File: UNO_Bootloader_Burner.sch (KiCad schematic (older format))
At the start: 12 parts, among them J1 Conn_01x06_Female, J2 Conn_01x06_Female, U1 ATmega328-AU-MCU_Microchip_AT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, Y1 Crystal_GND24

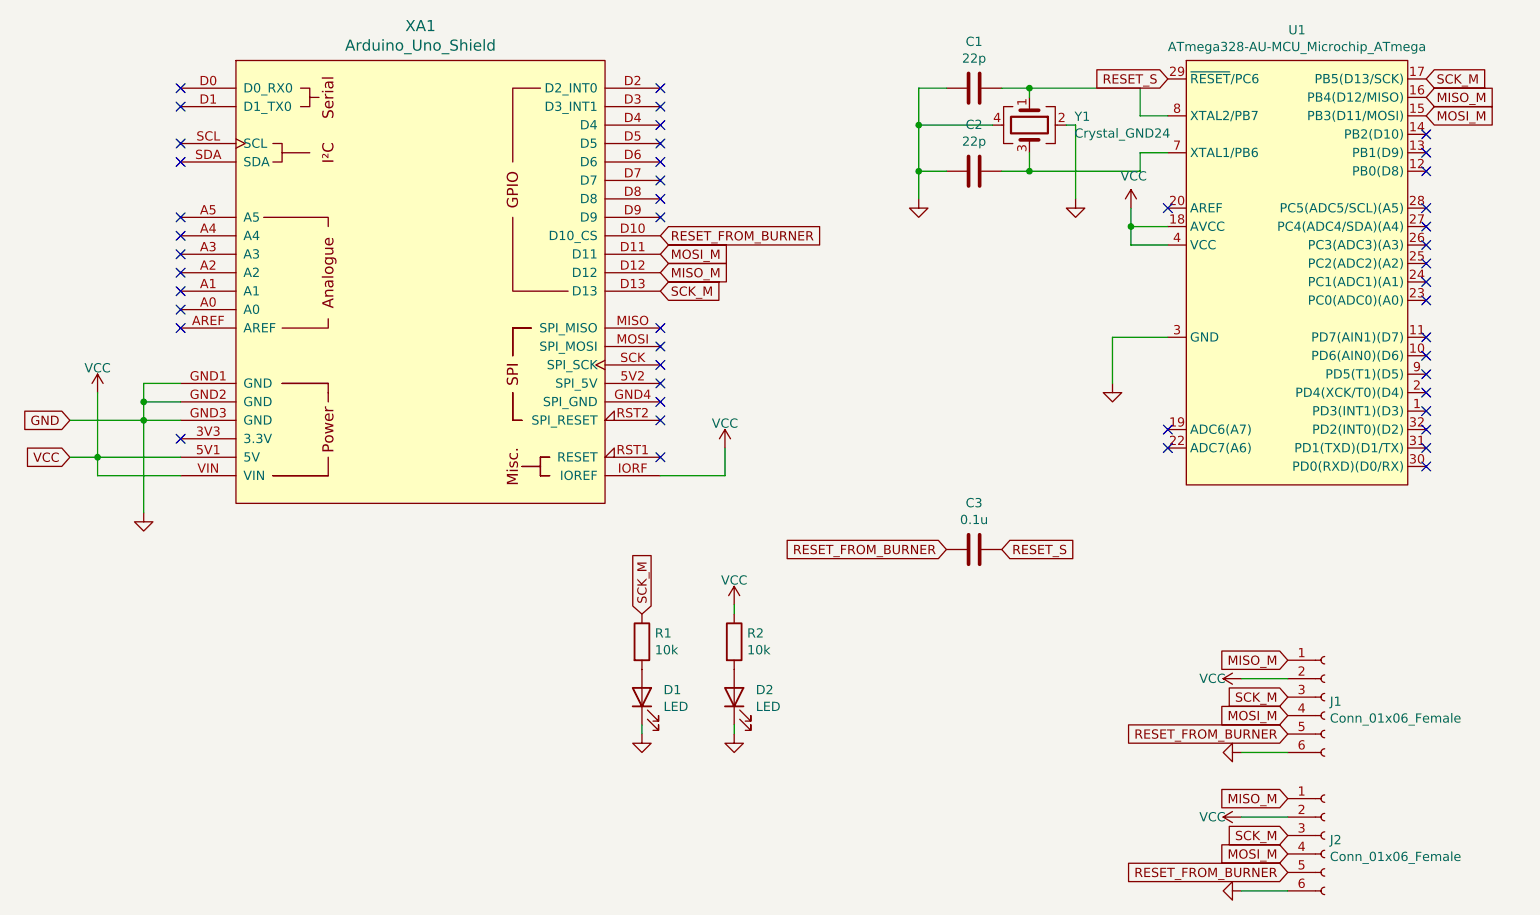
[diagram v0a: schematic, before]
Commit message: add QR CODE to the PCB file
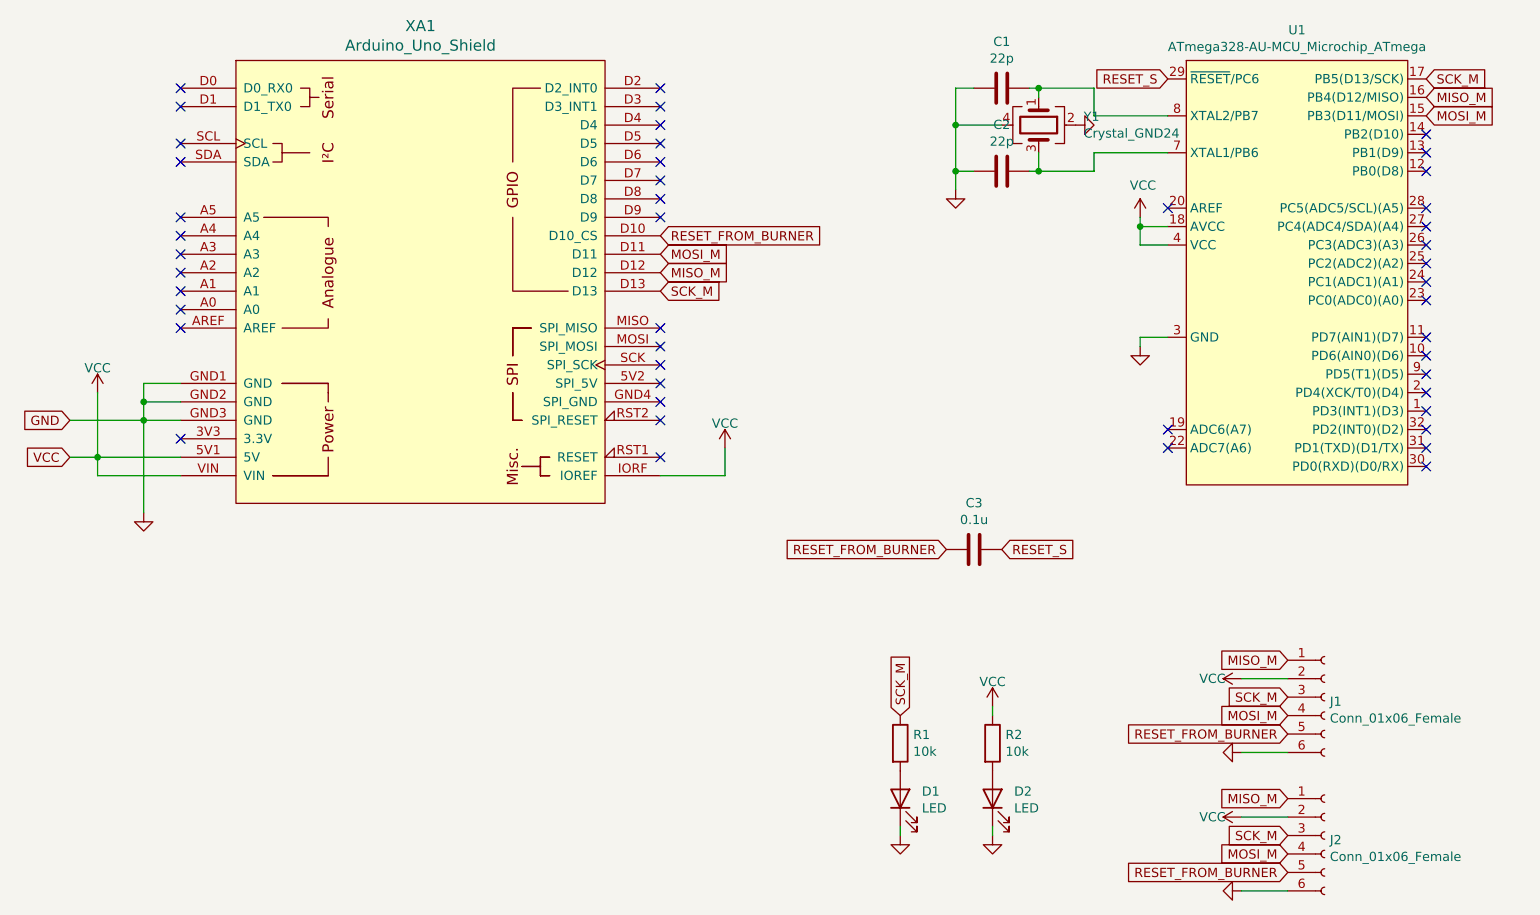
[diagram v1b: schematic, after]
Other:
- moved on the sheet: C1, C2, D1, D2, R1, R2, Y1
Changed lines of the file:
@@
 NoConn ~ 5200 3050
 NoConn ~ 5200 2950
-$Comp
-L Device:Crystal_GND24 Y1
-U 1 1 5FDB7F9F
-P 7200 1850
-F 0 "Y1" V 7154 2094 50  0000 L CNN
-F 1 "Crystal_GND24" V 7245 2094 50  0000 L CNN
-F 2 "Crystal:Crystal_SMD_3225-4Pin_3.2x2.5mm" H 7200 1850 50  0001 C CNN
-F 3 "~" H 7200 1850 50  0001 C CNN
-	1    7200 1850
-	0    1    1    0
-$EndComp
-Wire Wire Line
-	7200 1650 7800 1650
-Wire Wire Line
-	7800 1650 7800 1800
-Wire Wire Line
-	7800 1800 7950 1800
-Wire Wire Line
-	7950 2000 7800 2000
-Wire Wire Line
-	7800 2000 7800 2100
-Wire Wire Line
-	7800 2100 7200 2100
-Wire Wire Line
-	7200 2100 7200 2000
-Wire Wire Line
-	7200 1700 7200 1650
-Wire Wire Line
-	7400 1850 7450 1850
-Wire Wire Line
-	7450 1850 7450 2250
-$Comp
-L power:GND #PWR0104
-U 1 1 5FDBAF43
-P 7450 2250
-F 0 "#PWR0104" H 7450 2250 30  0001 C CNN
-F 1 "GND" H 7450 2180 30  0001 C CNN
-F 2 "" H 7450 2250 60  0000 C CNN
-F 3 "" H 7450 2250 60  0000 C CNN
-	1    7450 2250
-	1    0    0    -1
-$EndComp
-Wire Wire Line
-	7000 1850 6600 1850
-Wire Wire Line
-	6600 1850 6600 2100
+Wire Wire Line
+	7950 2000 7550 2000
+Wire Wire Line
+	7550 2000 7550 2100
+Wire Wire Line
+	7550 2100 7250 2100
 $Comp
 L power:GND #PWR0105
 U 1 1 5FDBB813
-P 6600 2250
-F 0 "#PWR0105" H 6600 2250 30  0001 C CNN
-F 1 "GND" H 6600 2180 30  0001 C CNN
-F 2 "" H 6600 2250 60  0000 C CNN
-F 3 "" H 6600 2250 60  0000 C CNN
-	1    6600 2250
+P 6800 2200
+F 0 "#PWR0105" H 6800 2200 30  0001 C CNN
+F 1 "GND" H 6800 2130 30  0001 C CNN
+F 2 "" H 6800 2200 60  0000 C CNN
+F 3 "" H 6800 2200 60  0000 C CNN
+	1    6800 2200
 	1    0    0    -1
 $EndComp
@@
 L Device:C C2
 U 1 1 5FDBBA3E
-P 6900 2100
-F 0 "C2" V 6648 2100 50  0000 C CNN
-F 1 "22p" V 6739 2100 50  0000 C CNN
-F 2 "Capacitor_SMD:C_0603_1608Metric" H 6938 1950 50  0001 C CNN
-F 3 "~" H 6900 2100 50  0001 C CNN
-	1    6900 2100
-	0    1    1    0
-$EndComp
-Wire Wire Line
-	7050 2100 7200 2100
-Connection ~ 7200 2100
-Wire Wire Line
-	6750 2100 6600 2100
-Connection ~ 6600 2100
-Wire Wire Line
-	6600 2100 6600 2250
-Wire Wire Line
-	6600 1850 6600 1650
-Wire Wire Line
-	6600 1650 6750 1650
-Connection ~ 6600 1850
+P 7050 2100
+F 0 "C2" V 6798 2100 50  0000 C CNN
+F 1 "22p" V 6889 2100 50  0000 C CNN
+F 2 "Capacitor_SMD:C_0603_1608Metric" H 7088 1950 50  0001 C CNN
+F 3 "~" H 7050 2100 50  0001 C CNN
+	1    7050 2100
+	0    1    1    0
+$EndComp
+Wire Wire Line
+	7200 2100 7250 2100
+Connection ~ 7250 2100
+Wire Wire Line
+	6900 2100 6800 2100
+Connection ~ 6800 2100
+Wire Wire Line
+	6800 2100 6800 2200
+Wire Wire Line
+	6800 1650 6900 1650
 $Comp
 L Device:C C1
 U 1 1 5FDBD493
-P 6900 1650
-F 0 "C1" V 6648 1650 50  0000 C CNN
-F 1 "22p" V 6739 1650 50  0000 C CNN
-F 2 "Capacitor_SMD:C_0603_1608Metric" H 6938 1500 50  0001 C CNN
-F 3 "~" H 6900 1650 50  0001 C CNN
-	1    6900 1650
-	0    1    1    0
-$EndComp
-Wire Wire Line
-	7050 1650 7200 1650
-Connection ~ 7200 1650
-Wire Wire Line
-	7950 3000 7650 3000
-Wire Wire Line
-	7650 3000 7650 3250
+P 7050 1650
+F 0 "C1" V 6798 1650 50  0000 C CNN
+F 1 "22p" V 6889 1650 50  0000 C CNN
+F 2 "Capacitor_SMD:C_0603_1608Metric" H 7088 1500 50  0001 C CNN
+F 3 "~" H 7050 1650 50  0001 C CNN
+	1    7050 1650
+	0    1    1    0
+$EndComp
+Wire Wire Line
+	7200 1650 7250 1650
+Connection ~ 7250 1650
+Wire Wire Line
+	7950 3000 7800 3000
+Wire Wire Line
+	7800 3000 7800 3050
 $Comp
 L power:GND #PWR0106
 U 1 1 5FDBECFC
-P 7650 3250
-F 0 "#PWR0106" H 7650 3250 30  0001 C CNN
-F 1 "GND" H 7650 3180 30  0001 C CNN
-F 2 "" H 7650 3250 60  0000 C CNN
-F 3 "" H 7650 3250 60  0000 C CNN
-	1    7650 3250
+P 7800 3050
+F 0 "#PWR0106" H 7800 3050 30  0001 C CNN
+F 1 "GND" H 7800 2980 30  0001 C CNN
+F 2 "" H 7800 3050 60  0000 C CNN
+F 3 "" H 7800 3050 60  0000 C CNN
+	1    7800 3050
 	1    0    0    -1
 $EndComp
@@
 L Device:R R2
 U 1 1 5FDC8A1B
-P 5600 4650
-F 0 "R2" H 5670 4696 50  0000 L CNN
-F 1 "10k" H 5670 4605 50  0000 L CNN
-F 2 "Resistor_SMD:R_0603_1608Metric" V 5530 4650 50  0001 C CNN
-F 3 "~" H 5600 4650 50  0001 C CNN
-	1    5600 4650
+P 7000 5200
+F 0 "R2" H 7070 5246 50  0000 L CNN
+F 1 "10k" H 7070 5155 50  0000 L CNN
+F 2 "Resistor_SMD:R_0603_1608Metric" V 6930 5200 50  0001 C CNN
+F 3 "~" H 7000 5200 50  0001 C CNN
+	1    7000 5200
 	1    0    0    -1
 $EndComp
@@
 L Device:LED D2
 U 1 1 5FDC9386
-P 5600 4950
-F 0 "D2" V 5639 4833 50  0000 R CNN
-F 1 "LED" V 5548 4833 50  0000 R CNN
-F 2 "LED_SMD:LED_0603_1608Metric" H 5600 4950 50  0001 C CNN
-F 3 "~" H 5600 4950 50  0001 C CNN
-	1    5600 4950
+P 7000 5500
+F 0 "D2" V 7039 5383 50  0000 R CNN
+F 1 "LED" V 6948 5383 50  0000 R CNN
+F 2 "LED_SMD:LED_0603_1608Metric" H 7000 5500 50  0001 C CNN
+F 3 "~" H 7000 5500 50  0001 C CNN
+	1    7000 5500
 	0    -1   -1   0
 $EndComp
@@
 $EndComp
 Wire Wire Line
-	5600 4500 5600 4450
+	7000 5050 7000 5000
 $Comp
 L power:VCC #PWR0111
 U 1 1 5FDCC106
-P 5600 4450
-F 0 "#PWR0111" H 5600 4500 30  0001 C CNN
-F 1 "VCC" H 5600 4583 50  0000 C CNN
-F 2 "" H 5600 4450 60  0000 C CNN
-F 3 "" H 5600 4450 60  0000 C CNN
-	1    5600 4450
-	1    0    0    -1
-$EndComp
-Wire Wire Line
-	5600 5100 5600 5150
+P 7000 5000
+F 0 "#PWR0111" H 7000 5050 30  0001 C CNN
+F 1 "VCC" H 7000 5133 50  0000 C CNN
+F 2 "" H 7000 5000 60  0000 C CNN
+F 3 "" H 7000 5000 60  0000 C CNN
+	1    7000 5000
+	1    0    0    -1
+$EndComp
+Wire Wire Line
+	7000 5650 7000 5700
 $Comp
 L power:GND #PWR0112
 U 1 1 5FDCCEBE
-P 5600 5150
-F 0 "#PWR0112" H 5600 5150 30  0001 C CNN
-F 1 "GND" H 5600 5080 30  0001 C CNN
-F 2 "" H 5600 5150 60  0000 C CNN
-F 3 "" H 5600 5150 60  0000 C CNN
-	1    5600 5150
+P 7000 5700
+F 0 "#PWR0112" H 7000 5700 30  0001 C CNN
+F 1 "GND" H 7000 5630 30  0001 C CNN
+F 2 "" H 7000 5700 60  0000 C CNN
+F 3 "" H 7000 5700 60  0000 C CNN
+	1    7000 5700
 	1    0    0    -1
 $EndComp
@@
 L Device:R R1
 U 1 1 5FDD35A7
-P 5100 4650
-F 0 "R1" H 5170 4696 50  0000 L CNN
-F 1 "10k" H 5170 4605 50  0000 L CNN
-F 2 "Resistor_SMD:R_0603_1608Metric" V 5030 4650 50  0001 C CNN
-F 3 "~" H 5100 4650 50  0001 C CNN
-	1    5100 4650
+P 6500 5200
+F 0 "R1" H 6570 5246 50  0000 L CNN
+F 1 "10k" H 6570 5155 50  0000 L CNN
+F 2 "Resistor_SMD:R_0603_1608Metric" V 6430 5200 50  0001 C CNN
+F 3 "~" H 6500 5200 50  0001 C CNN
+	1    6500 5200
 	1    0    0    -1
 $EndComp
@@
 L Device:LED D1
 U 1 1 5FDD35AD
-P 5100 4950
-F 0 "D1" V 5139 4833 50  0000 R CNN
-F 1 "LED" V 5048 4833 50  0000 R CNN
-F 2 "LED_SMD:LED_0603_1608Metric" H 5100 4950 50  0001 C CNN
-F 3 "~" H 5100 4950 50  0001 C CNN
-	1    5100 4950
-	0    -1   -1   0
-$EndComp
-Wire Wire Line
-	5100 5100 5100 5150
+P 6500 5500
+F 0 "D1" V 6539 5383 50  0000 R CNN
+F 1 "LED" V 6448 5383 50  0000 R CNN
+F 2 "LED_SMD:LED_0603_1608Metric" H 6500 5500 50  0001 C CNN
+F 3 "~" H 6500 5500 50  0001 C CNN
+	1    6500 5500
+	0    -1   -1   0
+$EndComp
+Wire Wire Line
+	6500 5650 6500 5700
 $Comp
 L power:GND #PWR0113
 U 1 1 5FDD35BB
-P 5100 5150
-F 0 "#PWR0113" H 5100 5150 30  0001 C CNN
-F 1 "GND" H 5100 5080 30  0001 C CNN
-F 2 "" H 5100 5150 60  0000 C CNN
-F 3 "" H 5100 5150 60  0000 C CNN
-	1    5100 5150
-	1    0    0    -1
-$EndComp
-Text GLabel 5100 4500 1    50   Input ~ 0
+P 6500 5700
+F 0 "#PWR0113" H 6500 5700 30  0001 C CNN
+F 1 "GND" H 6500 5630 30  0001 C CNN
+F 2 "" H 6500 5700 60  0000 C CNN
+F 3 "" H 6500 5700 60  0000 C CNN
+	1    6500 5700
+	1    0    0    -1
+$EndComp
+Text GLabel 6500 5050 1    50   Input ~ 0
 SCK_M
 Text GLabel 9350 1600 2    50   Input ~ 0
@@
 MISO_M
 Wire Wire Line
-	7950 2400 7750 2400
-Wire Wire Line
-	7750 2400 7750 2300
+	7950 2400 7800 2400
+Wire Wire Line
+	7800 2400 7800 2350
 $Comp
 L power:VCC #PWR?
 U 1 1 5FDBE539
-P 7750 2300
-F 0 "#PWR?" H 7750 2150 50  0001 C CNN
-F 1 "VCC" H 7765 2473 50  0000 C CNN
-F 2 "" H 7750 2300 50  0001 C CNN
-F 3 "" H 7750 2300 50  0001 C CNN
-	1    7750 2300
-	1    0    0    -1
-$EndComp
-Wire Wire Line
-	7750 2400 7750 2500
-Wire Wire Line
-	7750 2500 7950 2500
-Connection ~ 7750 2400
+P 7800 2350
+F 0 "#PWR?" H 7800 2200 50  0001 C CNN
+F 1 "VCC" H 7815 2523 50  0000 C CNN
+F 2 "" H 7800 2350 50  0001 C CNN
+F 3 "" H 7800 2350 50  0001 C CNN
+	1    7800 2350
+	1    0    0    -1
+$EndComp
+Wire Wire Line
+	7800 2400 7800 2500
+Wire Wire Line
+	7800 2500 7950 2500
+Connection ~ 7800 2400
+Wire Wire Line
+	7250 2100 7250 2000
+$Comp
+L power:GND #PWR0104
+U 1 1 5FDBAF43
+P 7450 1850
+F 0 "#PWR0104" H 7450 1850 30  0001 C CNN
+F 1 "GND" H 7450 1780 30  0001 C CNN
+F 2 "" H 7450 1850 60  0000 C CNN
+F 3 "" H 7450 1850 60  0000 C CNN
+	1    7450 1850
+	0    -1   -1   0
+$EndComp
+Wire Wire Line
+	7250 1700 7250 1650
+Wire Wire Line
+	6800 1850 6800 1650
+Wire Wire Line
+	6800 1850 6800 2100
+Connection ~ 6800 1850
+$Comp
+L Device:Crystal_GND24 Y1
+U 1 1 5FDB7F9F
+P 7250 1850
+F 0 "Y1" V 7204 2094 50  0000 L CNN
+F 1 "Crystal_GND24" V 7295 2094 50  0000 L CNN
+F 2 "Crystal:Crystal_SMD_3225-4Pin_3.2x2.5mm" H 7250 1850 50  0001 C CNN
+F 3 "~" H 7250 1850 50  0001 C CNN
+	1    7250 1850
+	0    1    1    0
+$EndComp
+Wire Wire Line
+	7050 1850 6800 1850
+Wire Wire Line
+	7550 1650 7550 1800
+Wire Wire Line
+	7550 1800 7950 1800
+Wire Wire Line
+	7250 1650 7550 1650
 $EndSCHEMATC

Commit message: update library path
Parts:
- U1: symbol controller-rescue:ATmega328-AU-MCU_Microchip_ATmega -> UNO_Bootloader_Burner-rescue:ATmega328-AU-MCU_Microchip_ATmega-controller-rescue
- XA1: symbol arduino:Arduino_Uno_Shield -> UNO_Bootloader_Burner-rescue:Arduino_Uno_Shield-arduino
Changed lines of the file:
@@
 $EndDescr
 $Comp
-L controller-rescue:ATmega328-AU-MCU_Microchip_ATmega U1
+L UNO_Bootloader_Burner-rescue:ATmega328-AU-MCU_Microchip_ATmega-controller-rescue U1
 U 1 1 5FDA5711
 P 8650 2750
@@
 RESET_FROM_BURNER
 $Comp
-L arduino:Arduino_Uno_Shield XA1
+L UNO_Bootloader_Burner-rescue:Arduino_Uno_Shield-arduino XA1
 U 1 1 5FD9FE21
 P 3900 2700
